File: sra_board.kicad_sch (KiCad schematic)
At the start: 168 parts, among them J10 Conn_01x03_Pin, J11 Conn_01x08_Pin, J12 Conn_01x07_Pin, J13 Conn_01x04_Pin, J14 Conn_01x02_Pin, J15 Conn_01x02_Pin, J16 Conn_01x02_Pin, J17 USB_C_Receptacle_USB2.0_16P, J18 Conn_01x10_Pin, J19 Conn_01x10_Pin, J20 Conn_01x10_Pin, J3 Conn_01x03_Pin, J5 Conn_01x03_Pin, J6 Conn_01x03_Pin, J7 Conn_01x03_Pin, J8 Conn_01x03_Pin, J9 Conn_01x03_Pin, Q1 SS8050, Q2 SS8050, Q3 AO4435, Q4 AO4468, SW3 SW_IO0, SW4 Switch, SW5 SW_EN, SW6 Switch, U1 MAX7219CWG_T, U2 ESP32-WROOM-32E, U4 ME6211C33M5, U5 CH340C, U6 TPS562202, U7 CN3303, U8 TB6612FNG H-bridge Motor Driv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

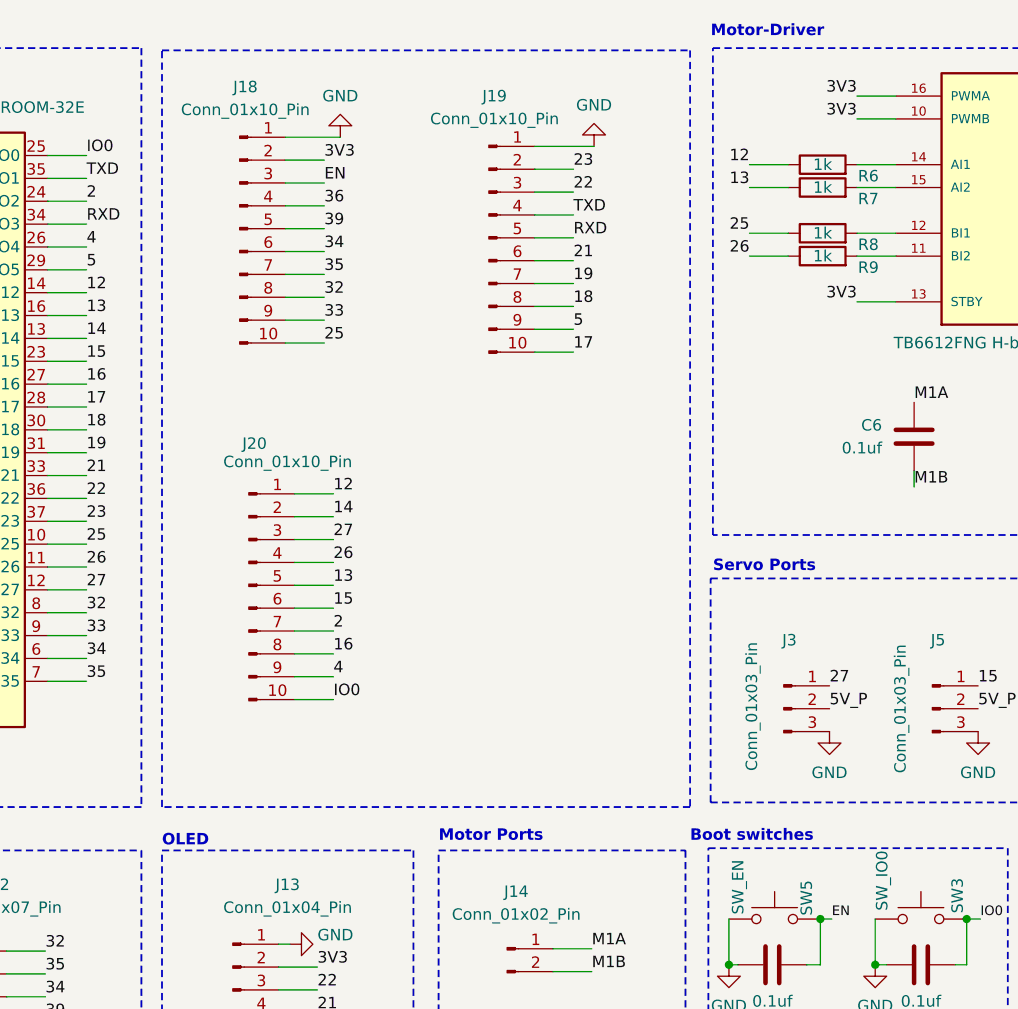
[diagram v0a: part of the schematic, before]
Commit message: Changed footprints
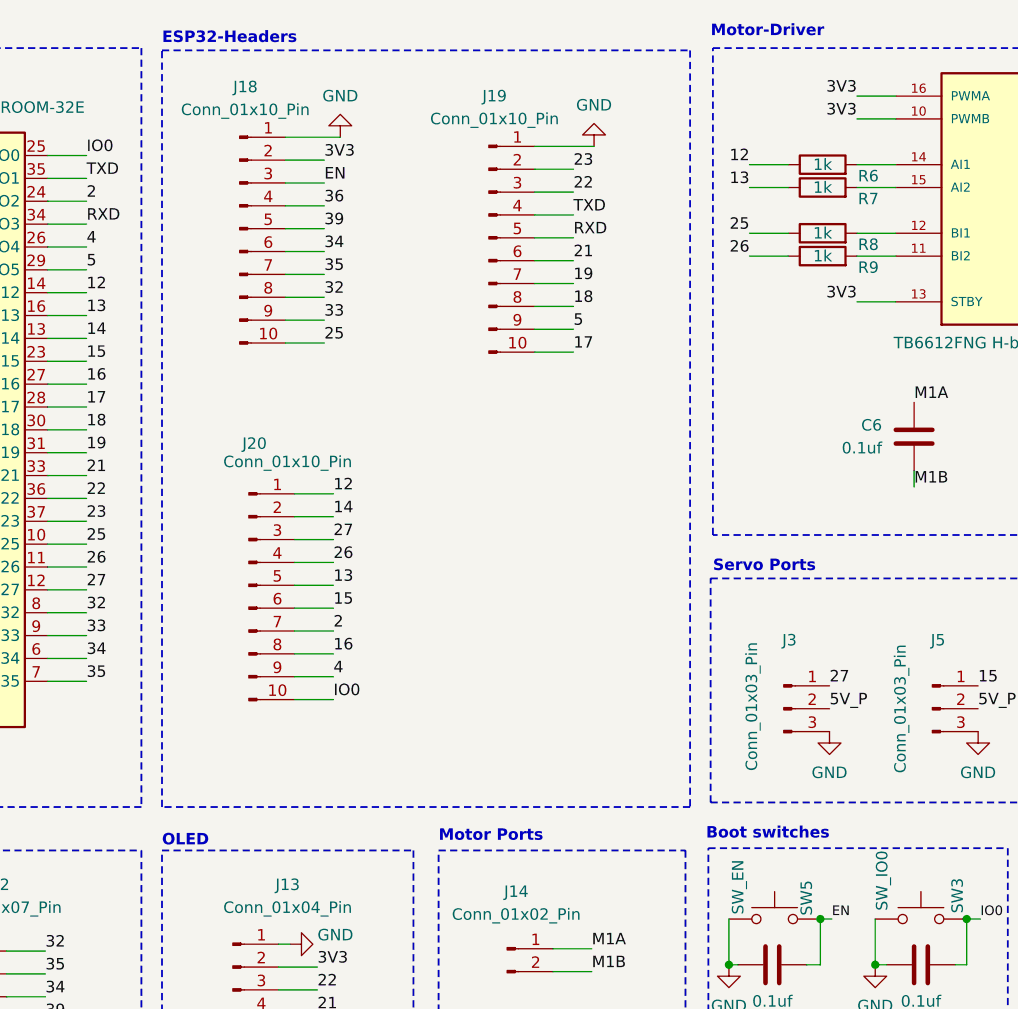
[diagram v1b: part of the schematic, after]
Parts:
- D73: footprint Diode_SMD:D_SMB -> Diode_SMD:D_SMA
- L1: footprint (none) -> Inductor_SMD:L_TDK_VLS6045EX_VLS6045AF
- U1: footprint MAX7219CWG_T:SOIC127P1032X265-24N -> max:SOIC24
- U7: footprint easyeda2kicad:SOP-8_L4.9-W3.9-P1.27-LS6.0-BL -> CN3303N:SOP-8_L4.9-W3.9-P1.27-LS6.0-BL
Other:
- note added: "ESP32-Headers"
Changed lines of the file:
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@@
 		)
 	)
+	(text "ESP32-Headers"
+		(exclude_from_sim no)
+		(at 73.66 16.51 0)
+		(effects
+			(font
+				(size 1.27 1.27)
+				(thickness 0.254)
+				(bold yes)
+			)
+			(justify left)
+		)
+	)
 	(text "Serial Boot\n"
 		(exclude_from_sim no)
@@
 	(text "Boot switches"
 		(exclude_from_sim no)
-		(at 132.334 105.156 0)
+		(at 134.112 104.902 0)
 		(effects
 			(font
@@
 			)
 		)
-		(property "Footprint" "MAX7219CWG_T:SOIC127P1032X265-24N"
+		(property "Footprint" "max:SOIC24"
 			(at 363.474 65.024 0)
 			(hide yes)
@@
 			)
 		)
-		(property "Footprint" ""
+		(property "Footprint" "Inductor_SMD:L_TDK_VLS6045EX_VLS6045AF"
 			(at 169.418 161.29 0)
 			(hide yes)
@@
 			)
 		)
-		(property "Footprint" "Diode_SMD:D_SMB"
+		(property "Footprint" "Diode_SMD:D_SMA"
 			(at 326.009 130.302 0)
 			(hide yes)
@@
 			)
 		)
-		(property "Footprint" "easyeda2kicad:SOP-8_L4.9-W3.9-P1.27-LS6.0-BL"
+		(property "Footprint" "CN3303N:SOP-8_L4.9-W3.9-P1.27-LS6.0-BL"
 			(at 145.034 186.69 0)
 			(hide yes)

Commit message: Made some arrengements
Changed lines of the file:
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@@
 	)
 	(rectangle
-		(start 200.406 145.288)
+		(start 200.406 145.034)
 		(end 279.654 202.692)
 		(stroke

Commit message: Made some placements
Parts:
- added J1: Conn_01x03_Pin, symbol Connector:Conn_01x03_Pin
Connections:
- net 5V_P: now also J1.1 (Pin_1)
- net Dout: now also J1.2 (Pin_2)
- net GND: now also J1.3 (Pin_3)
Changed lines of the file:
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@@
 	(wire
 		(pts
+			(xy 385.826 64.008) (xy 389.636 64.008)
+		)
+		(stroke
+			(width 0)
+			(type default)
+		)
+	)
+	(wire
+		(pts
 			(xy 86.614 124.714) (xy 90.932 124.714)
 		)
@@
 	(wire
 		(pts
+			(xy 389.636 61.468) (xy 385.826 61.468)
+		)
+		(stroke
+			(width 0)
+			(type default)
+		)
+	)
+	(wire
+		(pts
 			(xy 87.376 29.972) (xy 91.694 29.972)
 		)
@@
 	(wire
 		(pts
+			(xy 385.826 58.928) (xy 389.636 58.928)
+		)
+		(stroke
+			(width 0)
+			(type default)
+		)
+	)
+	(wire
+		(pts
 			(xy 290.068 21.336) (xy 290.068 26.416)
 		)
@@
 		)
 	)
+	(label "5V_P"
+		(at 389.636 58.928 0)
+		(effects
+			(font
+				(size 1.27 1.27)
+			)
+			(justify left bottom)
+		)
+	)
 	(label "R4"
 		(at 341.63 70.104 180)
@@
 		)
 	)
+	(label "Dout"
+		(at 389.636 61.468 0)
+		(effects
+			(font
+				(size 1.27 1.27)
+			)
+			(justify left bottom)
+		)
+	)
 	(label "18"
 		(at 119.38 46.228 0)
@@
 	)
 	(symbol
+		(lib_id "power:GND")
+		(at 389.636 64.008 90)
+		(unit 1)
+		(body_style 1)
+		(exclude_from_sim no)
+		(in_bom yes)
+		(on_board yes)
+		(in_pos_files yes)
+		(dnp no)
+		(fields_autoplaced yes)
+		(property "Reference" "#PWR035"
+			(at 395.986 64.008 0)
+			(hide yes)
+			(show_name no)
+			(do_not_autoplace no)
+			(effects
+				(font
+					(size 1.27 1.27)
+				)
+			)
+		)
+		(property "Value" "GND"
+			(at 393.446 64.0079 90)
+			(show_name no)
+			(do_not_autoplace no)
+			(effects
+				(font
+					(size 1.27 1.27)
+				)
+				(justify right)
+			)
+		)
+		(property "Footprint" ""
+			(at 389.636 64.008 0)
+			(hide yes)
+			(show_name no)
+			(do_not_autoplace no)
+			(effects
+				(font
+					(size 1.27 1.27)
+				)
+			)
+		)
+		(property "Datasheet" ""
+			(at 389.636 64.008 0)
+			(hide yes)
+			(show_name no)
+			(do_not_autoplace no)
+			(effects
+				(font
+					(size 1.27 1.27)
+				)
+			)
+		)
+		(property "Description" "Power symbol creates a global label with name \"GND\" , ground"
+			(at 389.636 64.008 0)
+			(hide yes)
+			(show_name no)
+			(do_not_autoplace no)
+			(effects
+				(font
+					(size 1.27 1.27)
+				)
+			)
+		)
+		(pin "1"
+		)
+		(instances
+			(project "sra_board"
+				(path "/294e2e5f-a7b9-4d81-904c-b55cda9b730c"
+					(reference "#PWR035")
+					(unit 1)
+				)
+			)
+		)
+	)
+	(symbol
 		(lib_id "Motor Drivers:TB6612FNG H-bridge")
 		(at 170.434 35.56 0)
@@
 					(unit 1)
 				)
+			)
+		)
+	)
+	(symbol
+		(lib_id "Connector:Conn_01x03_Pin")
+		(at 380.746 61.468 0)
+		(unit 1)
+		(body_style 1)
+		(exclude_from_sim no)
+		(in_bom yes)
+		(on_board yes)
+		(in_pos_files yes)
+		(dnp no)
+		(property "Reference" "J1"
+			(at 384.048 55.626 0)
+			(show_name no)
+			(do_not_autoplace no)
+			(effects
+				(font
+					(size 1.27 1.27)
+				)
+			)
+		)
+		(property "Value" "Conn_01x03_Pin"
+			(at 378.46 61.214 90)
+			(show_name no)
+			(do_not_autoplace no)
+			(effects
+				(font
+					(size 1.27 1.27)
+				)
+			)
+		)
+		(property "Footprint" ""
+			(at 380.746 61.468 0)
+			(hide yes)
+			(show_name no)
+			(do_not_autoplace no)
+			(effects
+				(font
+					(size 1.27 1.27)
+				)
+			)
+		)
+		(property "Datasheet" ""
+			(at 380.746 61.468 0)
+			(hide yes)
+			(show_name no)
+			(do_not_autoplace no)
+			(effects
+				(font
+					(size 1.27 1.27)
+				)
+			)
+		)
+		(property "Description" "Generic connector, single row, 01x03, script generated"
+			(at 380.746 61.468 0)
+			(hide yes)
+			(show_name no)
+			(do_not_autoplace no)
+			(effects
+				(font
+					(size 1.27 1.27)
+				)
+			)
+		)
+		(pin "3"
+		)
+		(pin "2"
+		)
+		(pin "1"
+		)
+		(instances
+			(project "sra_board"
+				(path "/294e2e5f-a7b9-4d81-904c-b55cda9b730c"
+					(reference "J1")
+					(unit 1)
+				)

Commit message: Component Placement Done
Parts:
- removed J1: Conn_01x03_Pin, symbol Connector:Conn_01x03_Pin
- H1, H3, H5, H6: footprint MountingHole:MountingHole_3.2mm_M3_Pad_Via -> MountingHole:MountingHole_3.2mm_M3_DIN965_Pad
- H2, H4: footprint MountingHole:MountingHole_3.2mm_M3_Pad_Via -> MountingHole:MountingHole_3.2mm_M3
- SW4: footprint Button_Switch_THT:SW_Push_2P2T_Toggle_CK_PVA2OAH5xxxxxxV2 -> Button_Switch_SMD:SW_SPDT_PCM12
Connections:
- net 5V is gone; now on net 5V_P: C2.1, C3.1
- net 7v4 is gone; now on net 12V: TP3.1, U8.1 (VM)
- net 12V: now also U8.2 (VCC)
- net 3V3: no longer U8.2 (VCC)
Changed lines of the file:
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@@
 	)
 	(junction
-		(at 314.706 85.09)
-		(diameter 0)
-		(color 0 0 0 0)
-	)
-	(junction
 		(at 276.606 44.704)
 		(diameter 0)
@@
 	)
 	(junction
+		(at 314.706 85.09)
+		(diameter 0)
+		(color 0 0 0 0)
+	)
+	(junction
 		(at 274.574 37.084)
 		(diameter 0)
@@
 	(wire
 		(pts
-			(xy 385.826 64.008) (xy 389.636 64.008)
-		)
-		(stroke
-			(width 0)
-			(type default)
-		)
-	)
-	(wire
-		(pts
 			(xy 86.614 124.714) (xy 90.932 124.714)
 		)
@@
 	(wire
 		(pts
-			(xy 314.706 85.09) (xy 322.326 85.09)
-		)
-		(stroke
-			(width 0)
-			(type default)
-		)
-	)
-	(wire
-		(pts
 			(xy 299.1104 120.396) (xy 299.466 120.396)
 		)
@@
 	(wire
 		(pts
+			(xy 314.706 85.09) (xy 322.326 85.09)
+		)
+		(stroke
+			(width 0)
+			(type default)
+		)
+	)
+	(wire
+		(pts
 			(xy 291.846 54.61) (xy 299.466 54.61)
 		)
@@
 	(wire
 		(pts
-			(xy 389.636 61.468) (xy 385.826 61.468)
-		)
-		(stroke
-			(width 0)
-			(type default)
-		)
-	)
-	(wire
-		(pts
 			(xy 87.376 29.972) (xy 91.694 29.972)
 		)
@@
 	(wire
 		(pts
-			(xy 385.826 58.928) (xy 389.636 58.928)
-		)
-		(stroke
-			(width 0)
-			(type default)
-		)
-	)
-	(wire
-		(pts
 			(xy 290.068 21.336) (xy 290.068 26.416)
 		)
@@
 		)
 	)
+	(label "5V_P"
+		(at 381.762 69.088 0)
+		(effects
+			(font
+				(size 1.27 1.27)
+			)
+			(justify left bottom)
+		)
+	)
 	(label "R8"
 		(at 322.326 105.41 0)
@@
 		)
 	)
-	(label "3V3"
-		(at 189.992 22.86 0)
-		(effects
-			(font
-				(size 1.27 1.27)
-			)
-			(justify left bottom)
-		)
-	)
 	(label "5"
 		(at 119.38 48.768 0)
@@
 		)
 	)
+	(label "12V"
+		(at 189.992 25.4 0)
+		(effects
+			(font
+				(size 1.27 1.27)
+			)
+			(justify left bottom)
+		)
+	)
 	(label "C8"
 		(at 385.572 49.784 0)
@@
 		)
 	)
-	(label "5V_P"
-		(at 389.636 58.928 0)
-		(effects
-			(font
-				(size 1.27 1.27)
-			)
-			(justify left bottom)
-		)
-	)
 	(label "R4"
 		(at 341.63 70.104 180)
@@
 		)
 	)
-	(label "7v4"
-		(at 189.992 25.4 0)
-		(effects
-			(font
-				(size 1.27 1.27)
-			)
-			(justify left bottom)
-		)
-	)
 	(label "R5"
 		(at 341.63 75.184 180)
@@
 		)
 	)
-	(label "13"
-		(at 92.71 77.216 0)
+	(label "12V"
+		(at 189.992 22.86 0)
 		(effects
 			(font
@@
 		)
 	)
-	(label "Dout"
-		(at 389.636 61.468 0)
+	(label "13"
+		(at 92.71 77.216 0)
 		(effects
 			(font
@@
 		)
 	)
-	(label "5V"
-		(at 381.762 69.088 0)
-		(effects
-			(font
-				(size 1.27 1.27)
-			)
-			(justify left bottom)
-		)
-	)
 	(label "12"
 		(at 92.71 67.056 0)
@@
 			)
 		)
-		(property "Footprint" "MountingHole:MountingHole_3.2mm_M3_Pad_Via"
+		(property "Footprint" "MountingHole:MountingHole_3.2mm_M3_DIN965_Pad"
 			(at 367.03 118.872 0)
 			(hide yes)
@@
 	)
 	(symbol
-		(lib_id "power:GND")
-		(at 389.636 64.008 90)
-		(unit 1)
-		(body_style 1)
-		(exclude_from_sim no)
-		(in_bom yes)
-		(on_board yes)
-		(in_pos_files yes)
-		(dnp no)
-		(fields_autoplaced yes)
-		(property "Reference" "#PWR035"
-			(at 395.986 64.008 0)
-			(hide yes)
-			(show_name no)
-			(do_not_autoplace no)
-			(effects
-				(font
-					(size 1.27 1.27)
-				)
-			)
-		)
-		(property "Value" "GND"
-			(at 393.446 64.0079 90)
-			(show_name no)
-			(do_not_autoplace no)
-			(effects
-				(font
-					(size 1.27 1.27)
-				)
-				(justify right)
-			)
-		)
-		(property "Footprint" ""
-			(at 389.636 64.008 0)
-			(hide yes)
-			(show_name no)
-			(do_not_autoplace no)
-			(effects
-				(font
-					(size 1.27 1.27)
-				)
-			)
-		)
-		(property "Datasheet" ""
-			(at 389.636 64.008 0)
-			(hide yes)
-			(show_name no)
-			(do_not_autoplace no)
-			(effects
-				(font
-					(size 1.27 1.27)
-				)
-			)
-		)
-		(property "Description" "Power symbol creates a global label with name \"GND\" , ground"
-			(at 389.636 64.008 0)
-			(hide yes)
-			(show_name no)
-			(do_not_autoplace no)
-			(effects
-				(font
-					(size 1.27 1.27)
-				)
-			)
-		)
-		(pin "1"
-		)
-		(instances
-			(project "sra_board"
-				(path "/294e2e5f-a7b9-4d81-904c-b55cda9b730c"
-					(reference "#PWR035")
-					(unit 1)
-				)
-			)
-		)
-	)
-	(symbol
 		(lib_id "Motor Drivers:TB6612FNG H-bridge")
 		(at 170.434 35.56 0)
@@
 			)
 		)
-		(property "Footprint" "MountingHole:MountingHole_3.2mm_M3_Pad_Via"
+		(property "Footprint" "MountingHole:MountingHole_3.2mm_M3"
 			(at 367.284 126.746 0)
 			(hide yes)
@@
 			)
 		)
-		(property "Footprint" "MountingHole:MountingHole_3.2mm_M3_Pad_Via"
+		(property "Footprint" "MountingHole:MountingHole_3.2mm_M3_DIN965_Pad"
 			(at 367.538 134.366 0)
 			(hide yes)
@@
 			)
 		)
-		(property "Footprint" "MountingHole:MountingHole_3.2mm_M3_Pad_Via"
+		(property "Footprint" "MountingHole:MountingHole_3.2mm_M3_DIN965_Pad"
 			(at 388.112 118.872 0)
 			(hide yes)
@@
 			)
 		)
-		(property "Footprint" "MountingHole:MountingHole_3.2mm_M3_Pad_Via"
+		(property "Footprint" "MountingHole:MountingHole_3.2mm_M3_DIN965_Pad"
 			(at 388.874 134.62 0)
 			(hide yes)
@@
 			)
 		)
-		(property "Footprint" "Button_Switch_THT:SW_Push_2P2T_Toggle_CK_PVA2OAH5xxxxxxV2"
+		(property "Footprint" "Button_Switch_SMD:SW_SPDT_PCM12"
 			(at 304.546 120.396 0)
 			(hide yes)
@@
 	)
 	(symbol
-		(lib_id "Connector:Conn_01x03_Pin")
-		(at 380.746 61.468 0)
-		(unit 1)
-		(body_style 1)
-		(exclude_from_sim no)
-		(in_bom yes)
-		(on_board yes)
-		(in_pos_files yes)
-		(dnp no)
-		(property "Reference" "J1"
-			(at 384.048 55.626 0)
-			(show_name no)
-			(do_not_autoplace no)
-			(effects
-				(font
-					(size 1.27 1.27)
-				)
-			)
-		)
-		(property "Value" "Conn_01x03_Pin"
-			(at 378.46 61.214 90)
-			(show_name no)
-			(do_not_autoplace no)
-			(effects
-				(font
-					(size 1.27 1.27)
-				)
-			)
-		)
-		(property "Footprint" ""
-			(at 380.746 61.468 0)
-			(hide yes)
-			(show_name no)
-			(do_not_autoplace no)
-			(effects
-				(font
-					(size 1.27 1.27)
-				)
-			)
-		)
-		(property "Datasheet" ""
-			(at 380.746 61.468 0)
-			(hide yes)
-			(show_name no)
-			(do_not_autoplace no)
-			(effects
-				(font
-					(size 1.27 1.27)
-				)
-			)
-		)
-		(property "Description" "Generic connector, single row, 01x03, script generated"
-			(at 380.746 61.468 0)
-			(hide yes)
-			(show_name no)
-			(do_not_autoplace no)
-			(effects
-				(font
-					(size 1.27 1.27)
-				)
-			)
-		)
-		(pin "3"
-		)
-		(pin "2"
-		)
-		(pin "1"
-		)
-		(instances
-			(project "sra_board"
-				(path "/294e2e5f-a7b9-4d81-904c-b55cda9b730c"
-					(reference "J1")
-					(unit 1)
-				)
-			)
-		)
-	)
-	(symbol
 		(lib_id "Device:LED")
 		(at 268.986 101.6 90)
@@
 			)
 		)
-		(property "Footprint" "MountingHole:MountingHole_3.2mm_M3_Pad_Via"
+		(property "Footprint" "MountingHole:MountingHole_3.2mm_M3"
 			(at 388.62 126.492 0)
 			(hide yes)

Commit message: Done some routing
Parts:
- removed U6: TPS562202, Package_TO_SOT_SMD:SOT-563, symbol Regulator_Switching:TPS562202
- added U3: TPS562200, Package_TO_SOT_SMD:SOT-23-6, symbol Regulator_Switching:TPS562200
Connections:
- net 12V: now also U3.3 (VIN)
- net GND: now also U3.1 (GND)
- net at C16.1, L2.1: now also U3.2 (SW)
- net at C16.2: now also U3.6 (VBST)
- net at C15.1, R18.2, R19.2: now also U3.4 (VFB)
- net at R17.2: now also U3.5 (EN)
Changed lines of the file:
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@@
 	)
 	(symbol
-		(lib_id "Regulator_Switching:TPS562202")
-		(at 54.356 168.148 0)
-		(unit 1)
-		(body_style 1)
-		(exclude_from_sim no)
-		(in_bom yes)
-		(on_board yes)
-		(in_pos_files yes)
-		(dnp no)
-		(fields_autoplaced yes)
-		(property "Reference" "U6"
-			(at 54.356 157.988 0)
-			(show_name no)
-			(do_not_autoplace no)
-			(effects
-				(font
-					(size 1.27 1.27)
-				)
-			)
-		)
-		(property "Value" "TPS562202"
-			(at 54.356 160.528 0)
-			(show_name no)
-			(do_not_autoplace no)
-			(effects
-				(font
-					(size 1.27 1.27)
-				)
-			)
-		)
-		(property "Footprint" "Package_TO_SOT_SMD:SOT-563"
-			(at 55.626 174.498 0)
-			(hide yes)
-			(show_name no)
-			(do_not_autoplace no)
-			(effects
-				(font
-					(size 1.27 1.27)
-				)
-				(justify left)
-			)
-		)
-		(property "Datasheet" "https://www.ti.com/lit/gpn/tps562202"
-			(at 54.356 168.148 0)
-			(hide yes)
-			(show_name no)
-			(do_not_autoplace no)
-			(effects
-				(font
-					(size 1.27 1.27)
-				)
-			)
-		)
-		(property "Description" "2A Synchronous Step-Down Voltage Regulator 580kHz, adjustable output voltage, 4.5-17V Input Voltage, 0.804V-7V Output Voltage, SOT-563"
-			(at 54.356 168.148 0)
-			(hide yes)
-			(show_name no)
-			(do_not_autoplace no)
-			(effects
-				(font
-					(size 1.27 1.27)
-				)
-			)
-		)
-		(pin "3"
-		)
-		(pin "2"
-		)
-		(pin "4"
-		)
-		(pin "6"
-		)
-		(pin "5"
-		)
-		(pin "1"
-		)
-		(instances
-			(project "sra_board"
-				(path "/294e2e5f-a7b9-4d81-904c-b55cda9b730c"
-					(reference "U6")
-					(unit 1)
-				)
-			)
-		)
-	)
-	(symbol
 		(lib_id "Device:LED")
 		(at 307.086 30.226 90)
@@
 					(unit 1)
 				)
+			)
+		)
+	)
+	(symbol
+		(lib_id "Regulator_Switching:TPS562200")
+		(at 54.356 168.148 0)
+		(unit 1)
+		(body_style 1)
+		(exclude_from_sim no)
+		(in_bom yes)
+		(on_board yes)
+		(in_pos_files yes)
+		(dnp no)
+		(fields_autoplaced yes)
+		(property "Reference" "U3"
+			(at 54.356 158.242 0)
+			(show_name no)
+			(do_not_autoplace no)
+			(effects
+				(font
+					(size 1.27 1.27)
+				)
+			)
+		)
+		(property "Value" "TPS562200"
+			(at 54.356 160.782 0)
+			(show_name no)
+			(do_not_autoplace no)
+			(effects
+				(font
+					(size 1.27 1.27)
+				)
+			)
+		)
+		(property "Footprint" "Package_TO_SOT_SMD:SOT-23-6"
+			(at 55.626 174.498 0)
+			(hide yes)
+			(show_name no)
+			(do_not_autoplace no)
+			(effects
+				(font
+					(size 1.27 1.27)
+				)
+				(justify left)
+			)
+		)
+		(property "Datasheet" "http://www.ti.com/lit/ds/symlink/tps563200.pdf"
+			(at 54.356 168.148 0)
+			(hide yes)
+			(show_name no)
+			(do_not_autoplace no)
+			(effects
+				(font
+					(size 1.27 1.27)
+				)
+			)
+		)
+		(property "Description" "2A Synchronous Step-Down Voltage Regulator, Adjustable Output Voltage, 4.5-17V Input Voltage, SOT-23-6"
+			(at 54.356 168.148 0)
+			(hide yes)
+			(show_name no)
+			(do_not_autoplace no)
+			(effects
+				(font
+					(size 1.27 1.27)
+				)
+			)
+		)
+		(pin "3"
+		)
+		(pin "1"
+		)
+		(pin "6"
+		)
+		(pin "2"
+		)
+		(pin "4"
+		)
+		(pin "5"
+		)
+		(instances
+			(project "sra_board"
+				(path "/294e2e5f-a7b9-4d81-904c-b55cda9b730c"
+					(reference "U3")
+					(unit 1)
+				)
